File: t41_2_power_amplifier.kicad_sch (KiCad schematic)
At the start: 52 parts, among them J1 5-1814832-1, J2 5-1814832-1, J3 B2B-XH-A_LF__SN_, J5 Screw_Terminal_01x02, Q1 Q_NMOS_GSD, Q3 Q_NMOS_GSD, T1 Transformer_1P_SS, T2 Transformer_1P_1S, T3 Transformer_1P_1S, U1 MCP1802x-xx02xOT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

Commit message: Version 1.7, release version to fab.
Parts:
- removed U1: MCP1802x-xx02xOT, Package_TO_SOT_SMD:SOT-23-5, symbol 28F0121-0SR-10:MCP1802x-xx02xOT
- added R10: 2.2k, Resistor_SMD:R_1206_3216Metric, symbol 28F0121-0SR-10:R_Small_US
- added U3: MCP1804x-A002xOT, Package_TO_SOT_SMD:SOT-23-5, symbol Regulator_Linear:MCP1804x-A002xOT
- U2: footprint SOT-23-5_MC_MCH -> footprints:SOT-23-5_MC_MCH
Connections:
- net 12V_FIL: now also U3.1 (VIN)
- net 8V: now also U3.5 (VOUT)
- net GND: now also U2.4 (HYST), R10.1, U3.2 (GND); no longer R9.1
- net TXRX: no longer U2.4 (HYST)
- net at R3.2, U2.3 (*OUT): now also U3.4 (~{SHDN})
- new net: R10.2, R9.1
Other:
- note added: "10 VOLT BIAS REGULATOR"
- note added: "SET 2 DEGREES"
- note removed: "8 VOLT BIAS REGULATOR"
- note removed: "SET 10 DEGREES"

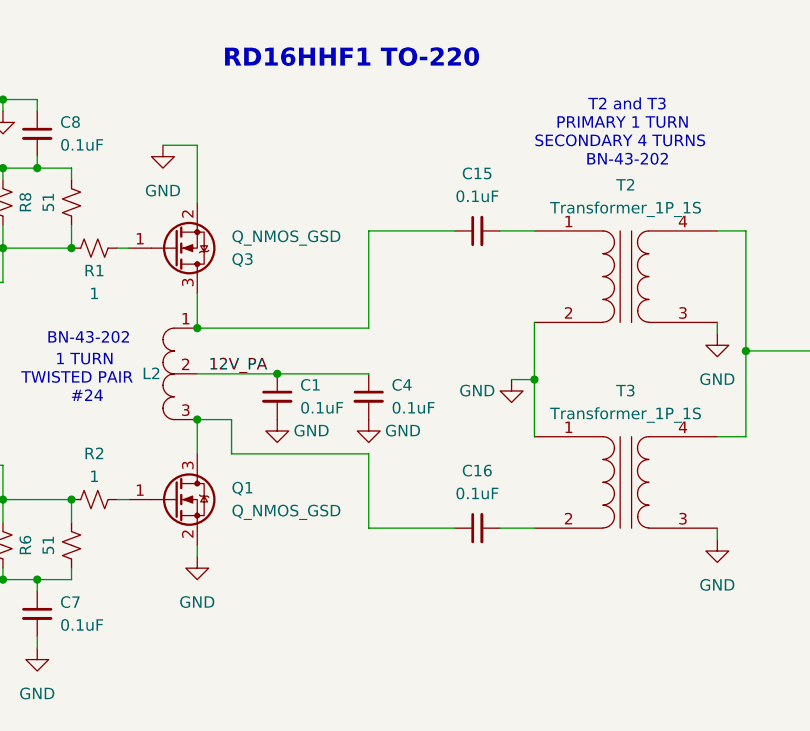
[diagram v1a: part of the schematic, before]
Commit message: Added output tuning capacitor.
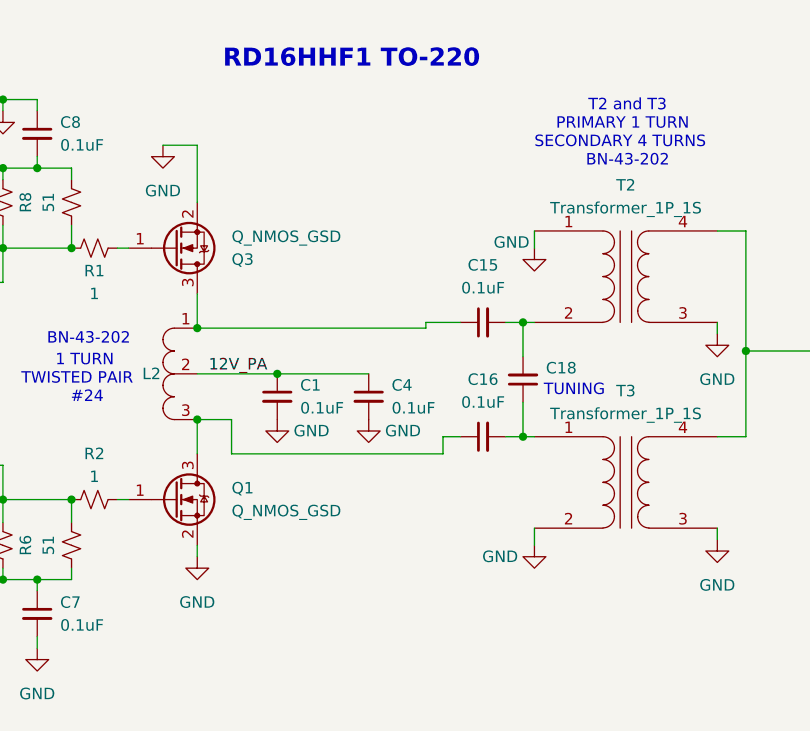
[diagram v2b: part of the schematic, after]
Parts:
- added C18: 0.1uF, Capacitor_SMD:C_1206_3216Metric, symbol 28F0121-0SR-10:C_Small
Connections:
- net GND: now also T2.1 (AA), T3.2 (AB); no longer T2.2 (AB), T3.1 (AA)
- net at C15.2: now also T2.2 (AB), C18.2; no longer T2.1 (AA)
- net at C16.2: now also T3.1 (AA), C18.1; no longer T3.2 (AB)
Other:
- note added: "TUNING"
- moved on the sheet: C15, C16

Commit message: Initial commit to Github.
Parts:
- R10: value 2.2k -> 0
- U2: value MCP9509CT-E/OT -> MCP9509HT-E/OT
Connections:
- net 8V renamed 10V
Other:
- note added: "1 TURN TWISTED PAIR #26"
- note added: "2 TURNS #26"
- note added: "2 TURNS TWISTED PAIR #24"
- note added: "R10 CAN BE ADJUSTED TO SET THRESHOLD TEMPERATURE"
- note added: "T2 and T3 PRIMARY 1 TURN #22 SECONDARY 4 TURNS #22 BN-43-202"
- note removed: "1 TURN TWISTED PAIR #24"
- note removed: "2 TURNS #24"
- note removed: "BN-43-202"
- note removed: "T2 and T3 PRIMARY 1 TURN SECONDARY 4 TURNS BN-43-202"
- moved on the sheet: C10, C11, C12, C13, C15, C16, C17, C18, C2, C3, C9, D1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
